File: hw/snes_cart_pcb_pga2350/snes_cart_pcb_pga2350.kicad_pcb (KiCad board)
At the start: 2 copper layers, 98.5 x 83 mm, 9 parts, among them J1 snescart_SNESCART_EXT, J2 Conn_02x02_Counter_Clockwise, J3 Conn_02x02_Counter_Clockwise, J4 Conn_02x08_Counter_Clockwise, J5 Conn_02x09_Counter_Clockwise, SW1 SW_Push, U1 PGA2350

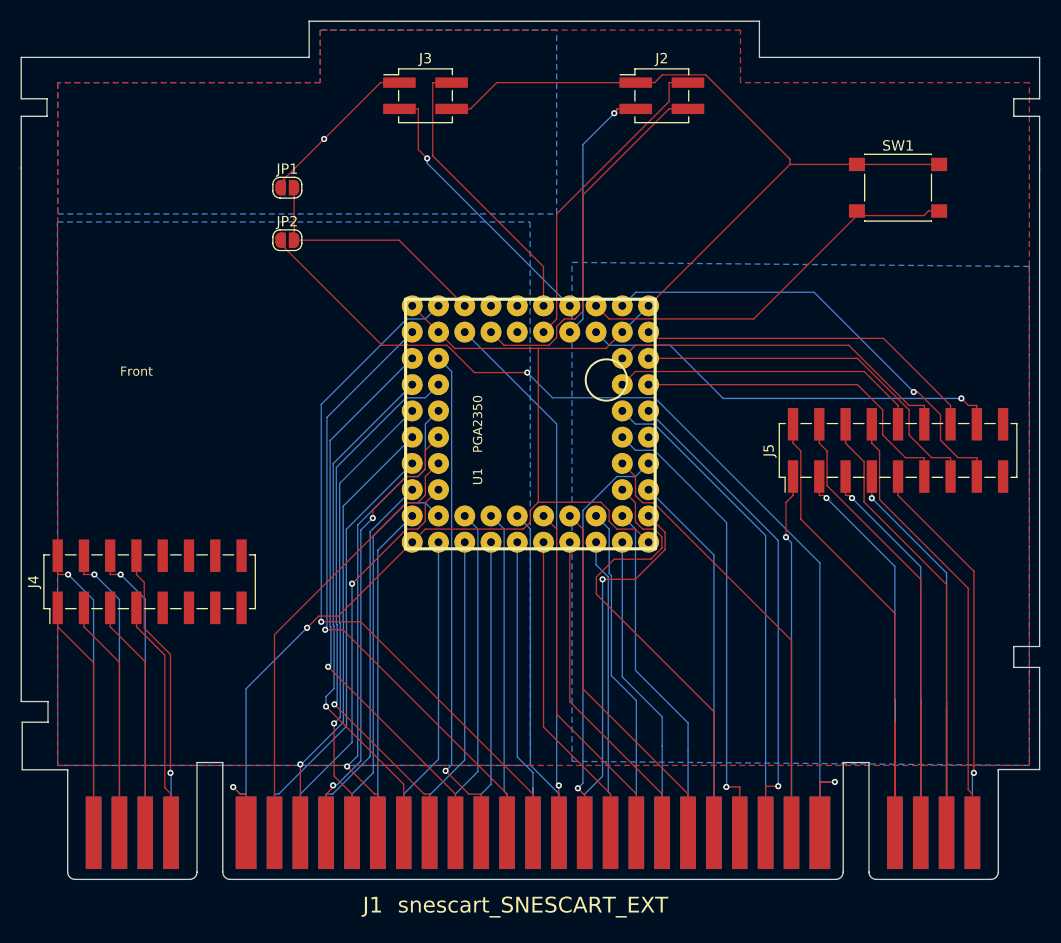
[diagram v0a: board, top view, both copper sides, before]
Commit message: (wip) initial support for cic on core1
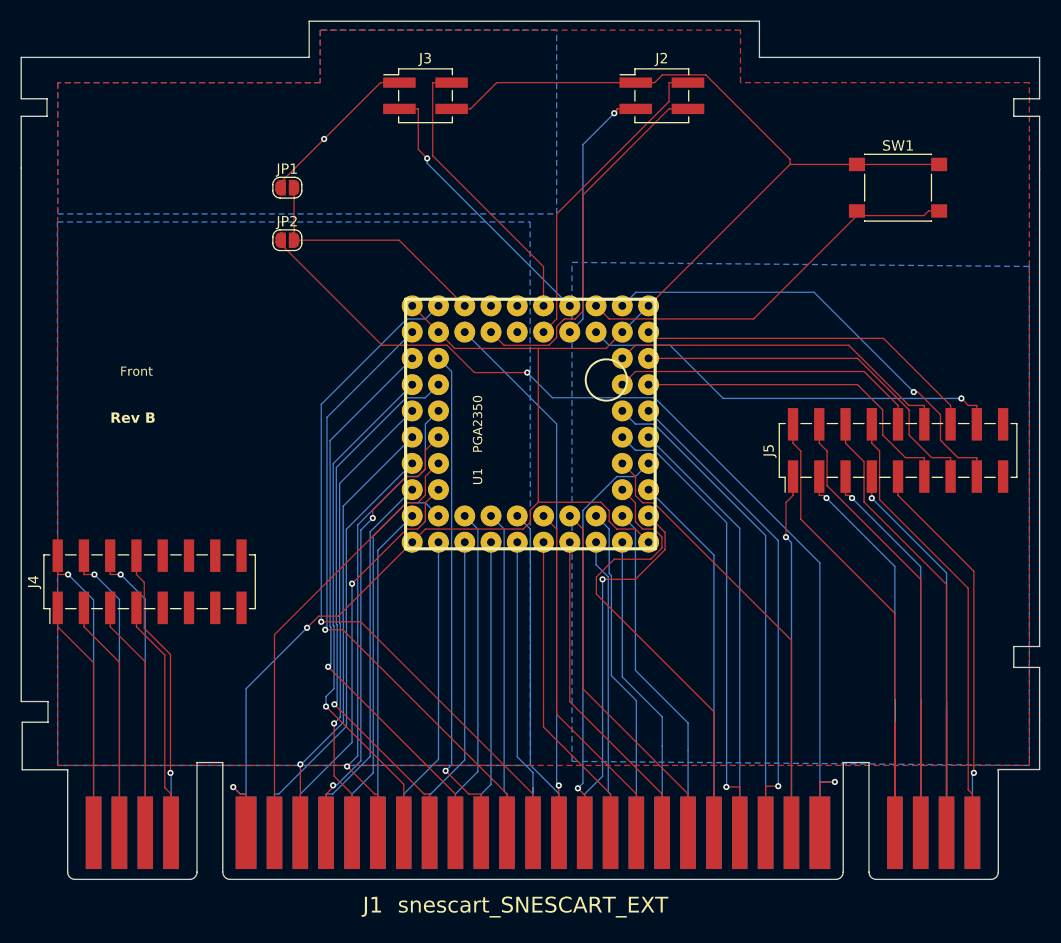
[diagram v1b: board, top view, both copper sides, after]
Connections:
- U1 pad F10: /CIC_P1_DIN -> /CIC_P2_DIN
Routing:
- net /CIC_P2_DIN: track 0.00 -> 41.9 mm
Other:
- board text added: "Rev B"
